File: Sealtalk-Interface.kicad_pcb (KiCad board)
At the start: 2 copper layers, 27 x 27 mm, 15 parts, among them J1 Screw_Terminal_01x02, J2 Screw_Terminal_01x02, J3 Conn_02x05_Counter_Clockwise, Q1 MMBT2222A, Q2 MMBT2222A, Q3 MMBT2907A, Q4 MMBT2222A

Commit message: Added jumper to configure Rx, fixed 2x5 header
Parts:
- added JP1: SolderJumper_3_Bridged12, Jumper:SolderJumper-3_P1.3mm_Bridged2Bar12_Pad1.0x1.5mm_NumberLabels, F.Cu at (124.8, 73.5)
- J3: value Conn_02x05_Counter_Clockwise -> Conn_02x05_Odd_Even
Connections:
- J3 pad 10: Net-(J3-Pad10) -> toRx
- J3 pad 4: Tx -> Net-(J3-Pad4)
- J3 pad 5: GND -> Net-(J3-Pad5)
- J3 pad 7: Rx -> GPIO
- J3 pad 8: Net-(J3-Pad8) -> Rx
- J3 pad 9: Net-(J3-Pad9) -> GND
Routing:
- net GPIO: track 0.00 -> 9.09 mm
- net Tx: track 25.6 -> 32.9 mm
- net toRx: track 0.00 -> 5.40 mm
- net Rx: track 18.1 -> 15.7 mm
- net Net-(Q1-Pad3): track 9.15 -> 9.80 mm

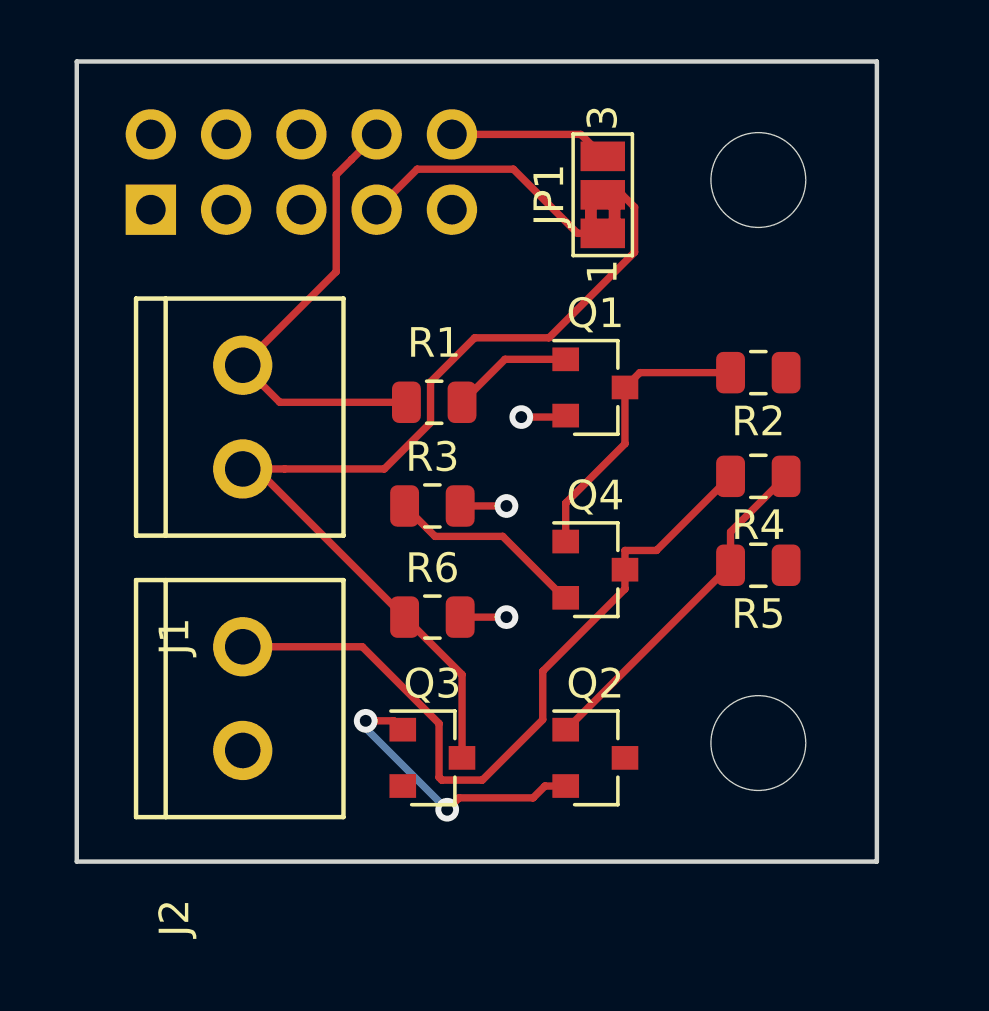
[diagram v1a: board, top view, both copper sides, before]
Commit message: Silk edits
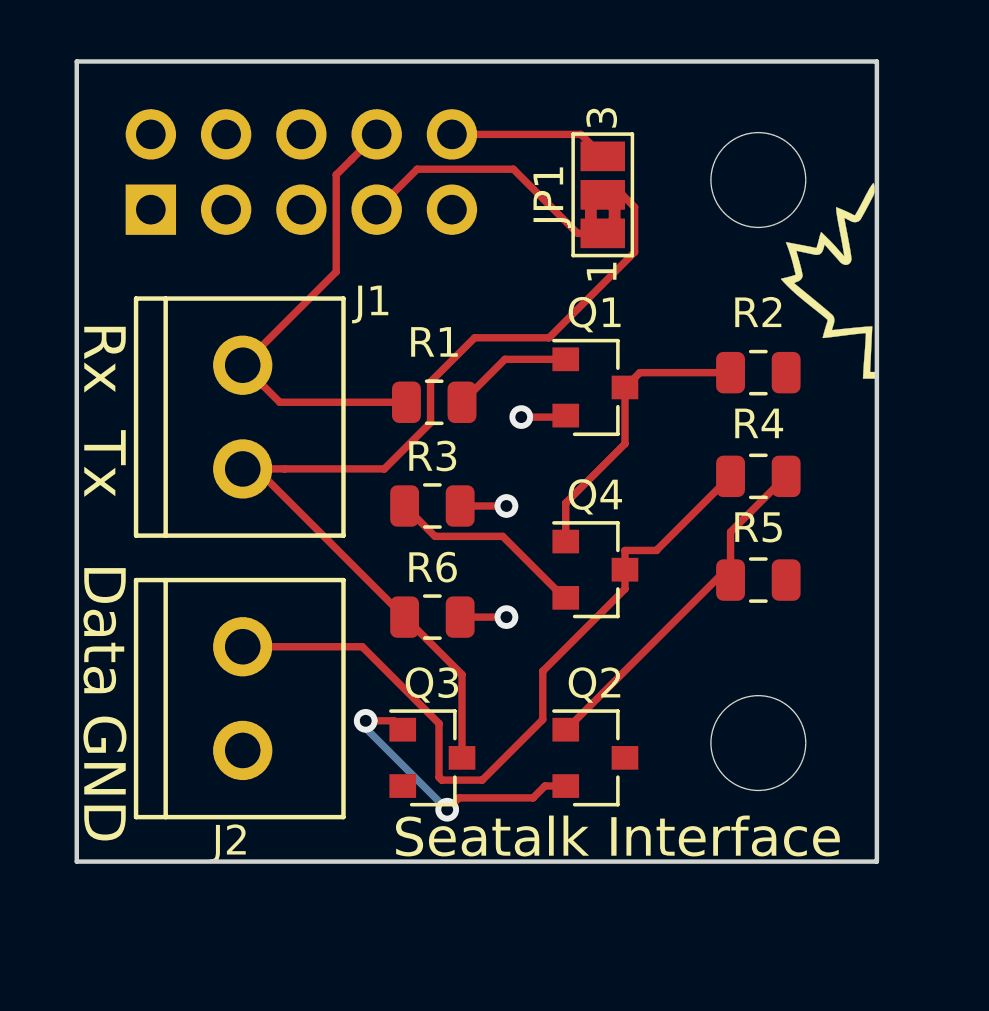
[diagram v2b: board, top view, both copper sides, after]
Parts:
- added G***: LOGO, Sealtalk-Interface:halfleaf, F.Cu at (132.4, 76.4)
- moved R5 0.50 mm to (130.0, 86.5)
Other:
- board text added: "Data"
- board text added: "GND"
- board text added: "GPIO"
- board text added: "RevA"
- board text added: "Rx"
- board text added: "Seatalk Interface"
- board text added: "Tx"
- board text added: "Usage info: http://github.com/ vintlabs/Seatalk-Interface"
- board text added: "Vcc"
- board text added: "VintLabs Seatalk Interface"

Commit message: RevB fixes
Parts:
- added R7: 10k, Resistor_SMD:R_0805_2012Metric, F.Cu at (130.1, 87.5)
- moved R5 2.00 mm to (130.1, 84.5)
- moved R4 1.50 mm to (130.1, 81.5)
- moved R2 1.00 mm to (130.1, 78.5)
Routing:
- net Net-(Q2-Pad2): track 9.84 -> 18.2 mm
- net Net-(Q2-Pad1): track 11.6 -> 13.2 mm
- net GND: track 4.65 -> 6.15 mm, vias 3 -> 4
- net SeatalkData: track 25.4 -> 26.3 mm
- net Net-(Q1-Pad3): track 9.80 -> 10.6 mm
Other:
- board text added: "RevB"
- board text removed: "RevA"
